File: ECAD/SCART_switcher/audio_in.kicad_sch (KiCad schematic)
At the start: 26 parts, among them Q25 BC847, Q26 BC847, Q27 2SK209, Q28 2SK209, U36 74LVC1G08, U37 CD4066

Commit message: Progressed ECAD.
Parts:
- renumbered C51 to C55, C52 to C56, C53 to C57, C54 to C58, C55 to C59, C56 to C60, R98 to R100, R99 to R101, R100 to R102, R101 to R103, R102 to R104, R103 to R105, R104 to R106, R92 to R94, R93 to R95, R94 to R96, R95 to R97, R96 to R98, R97 to R99, U36 to U37, U37 to U38

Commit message: Progressed ECAD.
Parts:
- renumbered C55 to C53, C56 to C54, C57 to C55, C58 to C56, C59 to C57, C60 to C58, R102 to R100, R103 to R101, R104 to R102, R105 to R103, R106 to R104, R94 to R92, R95 to R93, R96 to R94, R97 to R95, R98 to R96, R99 to R97, R100 to R98, R101 to R99

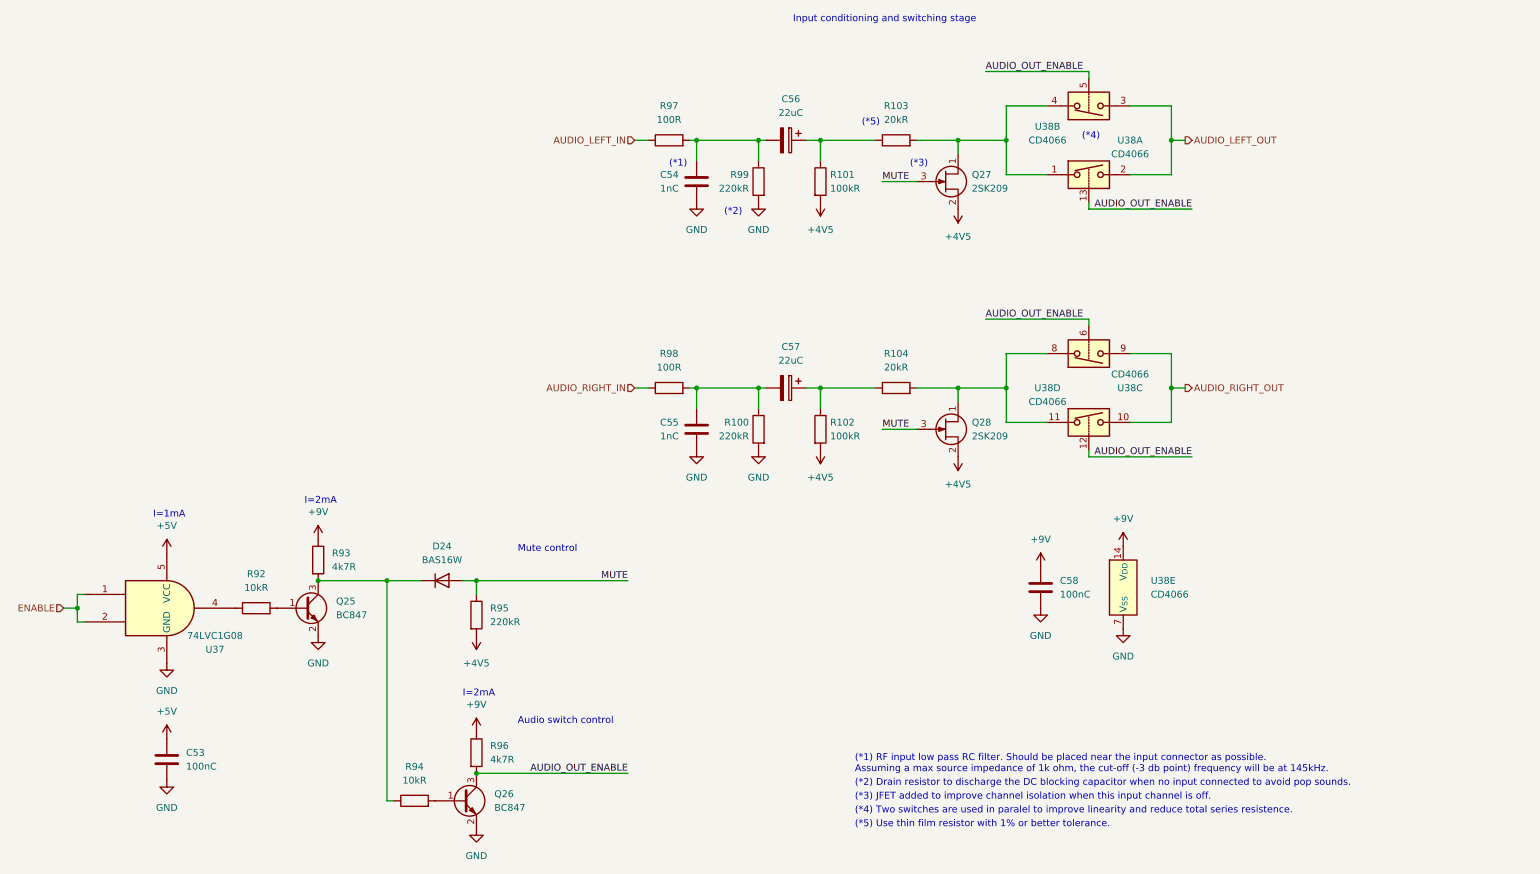
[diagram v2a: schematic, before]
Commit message: Cleanup and new power supply pcb
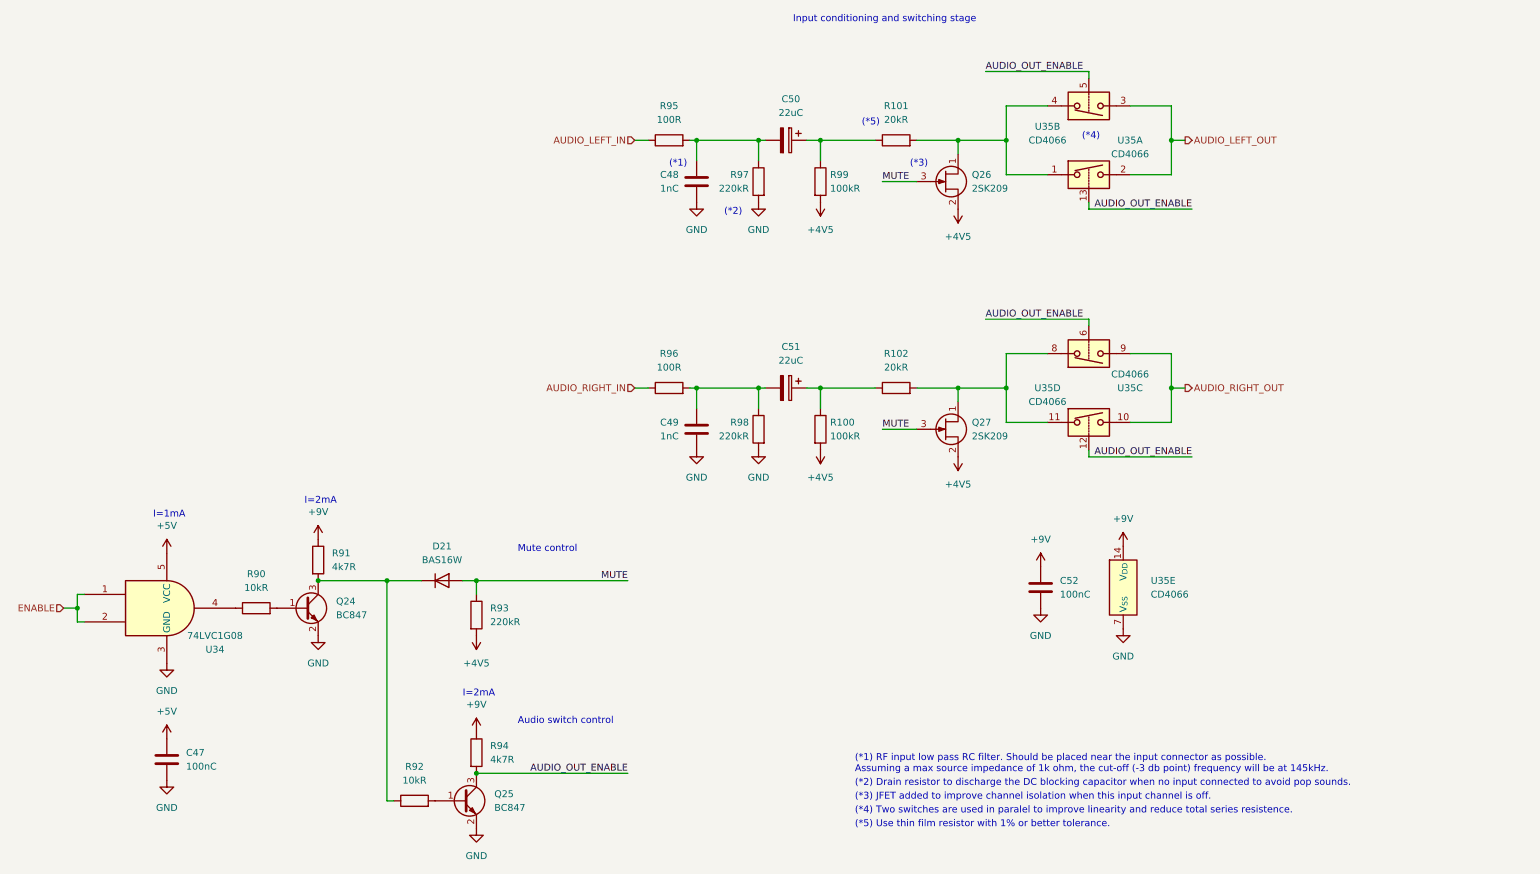
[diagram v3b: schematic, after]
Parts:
- renumbered C53 to C47, C54 to C48, C55 to C49, C56 to C50, C57 to C51, C58 to C52, D24 to D21, Q25 to Q24, Q26 to Q25, Q27 to Q26, Q28 to Q27, R102 to R100, R103 to R101, R104 to R102, R92 to R90, R93 to R91, R94 to R92, R95 to R93, R96 to R94, R97 to R95, R98 to R96, R99 to R97, R100 to R98, R101 to R99, U37 to U34, U38 to U35

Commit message: Progressed ECAD.
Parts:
- renumbered C47 to C45, C48 to C46, C49 to C47, C50 to C48, C51 to C49, C52 to C50

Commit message: Progressed ECAD.
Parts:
- renumbered R98 to R100, R99 to R101, R100 to R102, R101 to R103, R102 to R104, R90 to R92, R91 to R93, R92 to R94, R93 to R95, R94 to R96, R95 to R97, R96 to R98, R97 to R99

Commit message: Progressed ECAD.
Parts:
- R101, R102: MPN (none) -> RC0805FR-07100KL; Status (none) -> OK
- R92, R94: MPN RC0805FR-0710KL -> AC0805FR-0710KL; Status (none) -> OK
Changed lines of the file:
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@@
       (effects (font (size 1.27 1.27)) hide)
     )
-    (property "Datasheet" "https://datasheet.lcsc.com/lcsc/1810201611_YAGEO-RC0805FR-0710KL_C84376.pdf" (at 67.31 139.7 0)
-      (effects (font (size 1.27 1.27)) hide)
-    )
-    (property "MPN" "RC0805FR-0710KL" (at 67.31 139.7 0)
-      (effects (font (size 1.27 1.27)) hide)
-    )
-    (property "Status" "" (at 67.31 139.7 0)
+    (property "Datasheet" "https://datasheet.lcsc.com/lcsc/2304140030_YAGEO-AC0805FR-0710KL_C140868.pdf" (at 67.31 139.7 0)
+      (effects (font (size 1.27 1.27)) hide)
+    )
+    (property "MPN" "AC0805FR-0710KL" (at 67.31 139.7 0)
+      (effects (font (size 1.27 1.27)) hide)
+    )
+    (property "Status" "OK" (at 67.31 139.7 0)
       (effects (font (size 1.27 1.27)) hide)
     )
@@
       (effects (font (size 1.27 1.27)) hide)
     )
-    (property "Datasheet" "~" (at 171.45 60.96 0)
-      (effects (font (size 1.27 1.27)) hide)
-    )
-    (property "Status" "" (at 171.45 60.96 0)
+    (property "Datasheet" "https://datasheet.lcsc.com/lcsc/2304140030_YAGEO-RC0805FR-07100KL_C96346.pdf" (at 171.45 60.96 0)
+      (effects (font (size 1.27 1.27)) hide)
+    )
+    (property "Status" "OK" (at 171.45 60.96 0)
+      (effects (font (size 1.27 1.27)) hide)
+    )
+    (property "MPN" "RC0805FR-07100KL" (at 171.45 60.96 0)
       (effects (font (size 1.27 1.27)) hide)
     )
@@
       (effects (font (size 1.27 1.27)) hide)
     )
-    (property "Datasheet" "~" (at 171.45 106.68 0)
-      (effects (font (size 1.27 1.27)) hide)
-    )
-    (property "Status" "" (at 171.45 106.68 0)
+    (property "Datasheet" "https://datasheet.lcsc.com/lcsc/2304140030_YAGEO-RC0805FR-07100KL_C96346.pdf" (at 171.45 106.68 0)
+      (effects (font (size 1.27 1.27)) hide)
+    )
+    (property "Status" "OK" (at 171.45 106.68 0)
+      (effects (font (size 1.27 1.27)) hide)
+    )
+    (property "MPN" "RC0805FR-07100KL" (at 171.45 106.68 0)
       (effects (font (size 1.27 1.27)) hide)
     )
@@
       (effects (font (size 1.27 1.27)) hide)
     )
-    (property "Datasheet" "https://datasheet.lcsc.com/lcsc/1810201611_YAGEO-RC0805FR-0710KL_C84376.pdf" (at 96.52 175.26 0)
-      (effects (font (size 1.27 1.27)) hide)
-    )
-    (property "MPN" "RC0805FR-0710KL" (at 96.52 175.26 0)
-      (effects (font (size 1.27 1.27)) hide)
-    )
-    (property "Status" "" (at 96.52 175.26 0)
-      (effects (font (size 1.27 1.27)) hide)
-    )
+    (property "Datasheet" "https://datasheet.lcsc.com/lcsc/2304140030_YAGEO-AC0805FR-0710KL_C140868.pdf" (at 96.52 175.26 0)
+      (effects (font (size 1.27 1.27)) hide)
+    )
+    (property "MPN" "AC0805FR-0710KL" (at 96.52 175.26 0)
+      (effects (font (size 1.27 1.27)) hide)
+    )
+    (property "Status" "OK" (at 96.52 175.26 0)
+      (effects (font (size 1.27 1.27)) hide)
+    )

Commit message: Progressed ECAD.
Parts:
- C45: MPN CL21B104KBCNNNC -> CL10B104KO8NNNC; Status (none) -> OK
- C50: MPN (none) -> CL10B104KO8NNNC; Status (none) -> OK
- R100, R95, R99: MPN (none) -> RT0805DRD07220KL; Status (none) -> OK
- R103, R104: MPN (none) -> RT0805BRC0720KL; Status (none) -> OK
- R93, R96: MPN (none) -> RT0805FRE074K7L; Status (none) -> OK
- R97, R98: MPN (none) -> RT0805BRD07100RL; Status (none) -> OK
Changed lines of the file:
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@@
       (effects (font (size 1.27 1.27)) hide)
     )
-    (property "Datasheet" "~" (at 107.95 140.97 0)
-      (effects (font (size 1.27 1.27)) hide)
-    )
-    (property "Status" "" (at 107.95 140.97 0)
+    (property "Datasheet" "https://datasheet.lcsc.com/lcsc/2012011710_YAGEO-RT0805DRD07220KL_C706313.pdf" (at 107.95 140.97 0)
+      (effects (font (size 1.27 1.27)) hide)
+    )
+    (property "Status" "OK" (at 107.95 140.97 0)
+      (effects (font (size 1.27 1.27)) hide)
+    )
+    (property "MPN" "RT0805DRD07220KL" (at 107.95 140.97 0)
       (effects (font (size 1.27 1.27)) hide)
     )
@@
       (effects (font (size 1.27 1.27)) hide)
     )
-    (property "Datasheet" "~" (at 160.02 106.68 0)
-      (effects (font (size 1.27 1.27)) hide)
-    )
-    (property "Status" "" (at 160.02 106.68 0)
+    (property "Datasheet" "https://datasheet.lcsc.com/lcsc/2012011710_YAGEO-RT0805DRD07220KL_C706313.pdf" (at 160.02 106.68 0)
+      (effects (font (size 1.27 1.27)) hide)
+    )
+    (property "Status" "OK" (at 160.02 106.68 0)
+      (effects (font (size 1.27 1.27)) hide)
+    )
+    (property "MPN" "RT0805DRD07220KL" (at 160.02 106.68 0)
       (effects (font (size 1.27 1.27)) hide)
     )
@@
       (effects (font (size 1.27 1.27)) hide)
     )
-    (property "Datasheet" "https://datasheet.lcsc.com/lcsc/1810191215_Samsung-Electro-Mechanics-CL21B104KBCNNNC_C1711.pdf" (at 50.8 167.64 0)
-      (effects (font (size 1.27 1.27)) hide)
-    )
-    (property "MPN" "CL21B104KBCNNNC" (at 50.8 167.64 0)
-      (effects (font (size 1.27 1.27)) hide)
-    )
-    (property "Status" "" (at 50.8 167.64 0)
+    (property "Datasheet" "https://datasheet.lcsc.com/lcsc/1810271710_Samsung-Electro-Mechanics-CL10B104KO8NNNC_C66501.pdf" (at 50.8 167.64 0)
+      (effects (font (size 1.27 1.27)) hide)
+    )
+    (property "MPN" "CL10B104KO8NNNC" (at 50.8 167.64 0)
+      (effects (font (size 1.27 1.27)) hide)
+    )
+    (property "Status" "OK" (at 50.8 167.64 0)
       (effects (font (size 1.27 1.27)) hide)
     )
@@
       (effects (font (size 1.27 1.27)) hide)
     )
-    (property "Datasheet" "~" (at 185.42 99.06 0)
-      (effects (font (size 1.27 1.27)) hide)
-    )
-    (property "Status" "" (at 185.42 99.06 0)
+    (property "Datasheet" "https://datasheet.lcsc.com/lcsc/2009282137_YAGEO-RT0805BRC0720KL_C706206.pdf" (at 185.42 99.06 0)
+      (effects (font (size 1.27 1.27)) hide)
+    )
+    (property "Status" "OK" (at 185.42 99.06 0)
+      (effects (font (size 1.27 1.27)) hide)
+    )
+    (property "MPN" "RT0805BRC0720KL" (at 185.42 99.06 0)
       (effects (font (size 1.27 1.27)) hide)
     )
@@
       (effects (font (size 1.27 1.27)) hide)
     )
-    (property "Datasheet" "~" (at 78.74 130.81 0)
-      (effects (font (size 1.27 1.27)) hide)
-    )
-    (property "Status" "" (at 78.74 130.81 0)
+    (property "Datasheet" "https://datasheet.lcsc.com/lcsc/2010201810_YAGEO-RT0805FRE074K7L_C706390.pdf" (at 78.74 130.81 0)
+      (effects (font (size 1.27 1.27)) hide)
+    )
+    (property "Status" "OK" (at 78.74 130.81 0)
+      (effects (font (size 1.27 1.27)) hide)
+    )
+    (property "MPN" "RT0805FRE074K7L" (at 78.74 130.81 0)
       (effects (font (size 1.27 1.27)) hide)
     )
@@
       (effects (font (size 1.27 1.27)) hide)
     )
-    (property "Datasheet" "~" (at 143.51 53.34 0)
-      (effects (font (size 1.27 1.27)) hide)
-    )
-    (property "Status" "" (at 143.51 53.34 0)
+    (property "Datasheet" "https://datasheet.lcsc.com/lcsc/2304140030_YAGEO-RT0805BRD07100RL_C110773.pdf" (at 143.51 53.34 0)
+      (effects (font (size 1.27 1.27)) hide)
+    )
+    (property "Status" "OK" (at 143.51 53.34 0)
+      (effects (font (size 1.27 1.27)) hide)
+    )
+    (property "MPN" "RT0805BRD07100RL" (at 143.51 53.34 0)
       (effects (font (size 1.27 1.27)) hide)
     )
@@
       (effects (font (size 1.27 1.27)) hide)
     )
-    (property "Datasheet" "~" (at 160.02 60.96 0)
-      (effects (font (size 1.27 1.27)) hide)
-    )
-    (property "Status" "" (at 160.02 60.96 0)
+    (property "Datasheet" "https://datasheet.lcsc.com/lcsc/2012011710_YAGEO-RT0805DRD07220KL_C706313.pdf" (at 160.02 60.96 0)
+      (effects (font (size 1.27 1.27)) hide)
+    )
+    (property "Status" "OK" (at 160.02 60.96 0)
+      (effects (font (size 1.27 1.27)) hide)
+    )
+    (property "MPN" "RT0805DRD07220KL" (at 160.02 60.96 0)
       (effects (font (size 1.27 1.27)) hide)
     )
@@
       (effects (font (size 1.27 1.27)) hide)
     )
-    (property "Datasheet" "~" (at 185.42 53.34 0)
-      (effects (font (size 1.27 1.27)) hide)
-    )
-    (property "Status" "" (at 185.42 53.34 0)
+    (property "Datasheet" "https://datasheet.lcsc.com/lcsc/2009282137_YAGEO-RT0805BRC0720KL_C706206.pdf" (at 185.42 53.34 0)
+      (effects (font (size 1.27 1.27)) hide)
+    )
+    (property "Status" "OK" (at 185.42 53.34 0)
+      (effects (font (size 1.27 1.27)) hide)
+    )
+    (property "MPN" "RT0805BRC0720KL" (at 185.42 53.34 0)
       (effects (font (size 1.27 1.27)) hide)
     )
@@
       (effects (font (size 1.27 1.27)) hide)
     )
-    (property "Datasheet" "~" (at 107.95 166.37 0)
-      (effects (font (size 1.27 1.27)) hide)
-    )
-    (property "Status" "" (at 107.95 166.37 0)
+    (property "Datasheet" "https://datasheet.lcsc.com/lcsc/2010201810_YAGEO-RT0805FRE074K7L_C706390.pdf" (at 107.95 166.37 0)
+      (effects (font (size 1.27 1.27)) hide)
+    )
+    (property "Status" "OK" (at 107.95 166.37 0)
+      (effects (font (size 1.27 1.27)) hide)
+    )
+    (property "MPN" "RT0805FRE074K7L" (at 107.95 166.37 0)
       (effects (font (size 1.27 1.27)) hide)
     )
@@
       (effects (font (size 1.27 1.27)) hide)
     )
-    (property "Datasheet" "" (at 212.09 135.89 0)
-      (effects (font (size 1.27 1.27)) hide)
-    )
-    (property "MPN" "" (at 212.09 135.89 0)
-      (effects (font (size 1.27 1.27)) hide)
-    )
-    (property "Status" "" (at 212.09 135.89 0)
+    (property "Datasheet" "https://datasheet.lcsc.com/lcsc/1810271710_Samsung-Electro-Mechanics-CL10B104KO8NNNC_C66501.pdf" (at 212.09 135.89 0)
+      (effects (font (size 1.27 1.27)) hide)
+    )
+    (property "MPN" "CL10B104KO8NNNC" (at 212.09 135.89 0)
+      (effects (font (size 1.27 1.27)) hide)
+    )
+    (property "Status" "OK" (at 212.09 135.89 0)
       (effects (font (size 1.27 1.27)) hide)
     )
@@
       (effects (font (size 1.27 1.27)) hide)
     )
-    (property "Datasheet" "~" (at 143.51 99.06 0)
-      (effects (font (size 1.27 1.27)) hide)
-    )
-    (property "Status" "" (at 143.51 99.06 0)
-      (effects (font (size 1.27 1.27)) hide)
-    )
+    (property "Datasheet" "https://datasheet.lcsc.com/lcsc/2304140030_YAGEO-RT0805BRD07100RL_C110773.pdf" (at 143.51 99.06 0)
+      (effects (font (size 1.27 1.27)) hide)
+    )
+    (property "Status" "OK" (at 143.51 99.06 0)
+      (effects (font (size 1.27 1.27)) hide)
+    )
+    (property "MPN" "RT0805BRD07100RL" (at 143.51 99.06 0)
+      (effects (font (size 1.27 1.27)) hide)
+    )

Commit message: Progressed ECAD.
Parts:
- D71: renamed from D21; MPN_MOUSER (none) -> BAS16W,115
- Q24, Q25: MPN_MOUSER (none) -> BC847C,215
- Q26, Q27: MPN_MOUSER (none) -> MMBFJ113
- U34: MPN_MOUSER (none) -> SN74LVC1G08DCKR
- U35: MPN_MOUSER (none) -> CD4066BM96
